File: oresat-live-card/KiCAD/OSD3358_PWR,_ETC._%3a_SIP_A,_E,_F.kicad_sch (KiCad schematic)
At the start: 53 parts, among them Q1 MMBT2907, U10 TLVH431, U18 RCLAMP0504FB, U4 SN74LVC1G07DCK, U7 OSD3358-512M-BSM

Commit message: Schematic update for V1.2, still a few outstanding TODOs
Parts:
- TP102, TP109, TP110, TP112, TP121, TP129, TP130, TP132, TP136, TP14, TP140, TP145, TP150, TP151, TP154, TP155, TP156, TP157, TP160, TP161, TP164, TP165, TP166, TP167, TP172, TP173, TP2, TP25, TP3, TP4, TP9: footprint oresat-live-card:PAD.03X.04 -> oresat-live-card:2MM-TEST-POINT; symbol oresat-live-card-eagle-import:TEST-POINT3X4 -> oresat-live-card-eagle-import:TEST-POINT
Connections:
- net GND: now also U7.D8 (DGND@1), U7.D9 (DGND@2), U7.E10 (DGND@8), U7.E11 (DGND@9), U7.E12 (DGND@10), U7.E5 (DGND@3), U7.E6 (DGND@4), U7.E7 (DGND@5), U7.E8 (DGND@6), U7.E9 (DGND@7), U7.F12 (DGND@12), U7.F5 (DGND@11), U7.G12 (DGND@14), U7.G5 (DGND@13), U7.H12 (DGND@17), U7.H13 (DGND@18), U7.H4 (DGND@15), U7.H5 (DGND@16), U7.J12 (DGND@21), U7.J13 (DGND@22), U7.J4 (DGND@19), U7.J5 (DGND@20), U7.K12 (DGND@24), U7.K5 (DGND@23), U7.L12 (DGND@26), U7.L5 (DGND@25), U7.M10 (DGND@32), U7.M11 (DGND@33), U7.M12 (DGND@34), U7.M5 (DGND@27), U7.M6 (DGND@28), U7.M7 (DGND@29), U7.M8 (DGND@30), U7.M9 (DGND@31), U7.N8 (DGND@35), U7.N9 (DGND@36); no longer U7.F8 (SYS_VDD3_3P3V@1), U7.G8 (SYS_VDD3_3P3V@2), U7.G9 (VDDSHV5), U7.H8 (SYS_VDD3_3P3V@4), U7.H9 (VDDSHV6), U7.J7 (SYS_VDD3_3P3V@5), U7.J9 (VDDSHV1), U7.K8 (SYS_VDD3_3P3V@7), U7.K9 (VDDSHV2), U7.L4 (PMIC_NWAKEUP), U7.L8 (SYS_VDD3_3P3V@8), U7.L9 (VDDSHV3), U7.M13 (PMIC_NRESET), U7.N11 (PMIC_PWR_EN), U7.N4 (PMIC_LDO_PGOOD), U7.N5 (RTC_PWRONRSTN), U7.T11 (PMIC_PB_IN)
- net at TP154.1: now also U7.G4 (VDD_CORE)
- net at TP150.1: now also U7.J6 (NC@2)
- net at TP172.1: now also U7.D12 (NC@1)
- net at TP145.1: now also U7.K4 (NC@3)
- net at TP160.1: now also U7.F13 (VDD_MPU)
- net at TP157.1: now also U7.H6 (VPP)
- net at TP166.1: now also U7.G13 (VDDS_PLL)
- net at TP173.1: now also U7.D5 (CAP_VDD_RTC)
- net at TP156.1: now also U7.F4 (VDDS_DDR)

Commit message: BOM and minor cosmetic schematic updates
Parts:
- C13, C14: value 22uF -> 22u; symbol oresat-live-card-eagle-import:C-EUC1210 -> Device:C_Small; Distributor (none) -> DigiKey; MPN (none) -> CGA6P1X7R1C226M250AC
- C18, C41: value 0.1uF -> 100n; footprint oresat-live-card:.0603-A -> Resistor_SMD:R_0603_1608Metric; symbol oresat-live-card-eagle-import:C-EU0603-A -> Device:C_Small; Distributor (none) -> DigiKey; MPN (none) -> CL10B104KB8WPNC
- D1: Distributor (none) -> DigiKey; MPN (none) -> 150060GS75020
- Q1: Distributor (none) -> DigiKey; MPN (none) -> MMBT2907A-7-F
- R1: footprint oresat-live-card:.0603-A -> Resistor_SMD:R_0603_1608Metric; Distributor (none) -> DigiKey; MPN (none) -> ERJ-3EKF4701V
- R15, R28: footprint oresat-live-card:.0603-A -> Resistor_SMD:R_0603_1608Metric; Distributor (none) -> DigiKey; MPN (none) -> ERJ-3EKF1002V
- R23: footprint oresat-live-card:.0603-A -> Resistor_SMD:R_0603_1608Metric; Distributor (none) -> DigiKey; MPN (none) -> ERJ-3EKF4990V
- R31: footprint oresat-live-card:.0603-A -> Resistor_SMD:R_0603_1608Metric; Distributor (none) -> DigiKey; MPN (none) -> ERJ-3EKF4022V
- R73, R74, R75: footprint oresat-live-card:.0603-A -> Resistor_SMD:R_0603_1608Metric; Distributor (none) -> DigiKey; MPN (none) -> ERJ-3EKF1000V
- TP102, TP109, TP110, TP121, TP129, TP130, TP132, TP136, TP14, TP140, TP145, TP150, TP154, TP156, TP157, TP160, TP161, TP164, TP165, TP166, TP167, TP172, TP173, TP2, TP25, TP3, TP4, TP9: footprint oresat-live-card:2MM-TEST-POINT -> oresat-live-card:PAD.03X.04
- TP112, TP151, TP155: value TEST-POINT3X4 -> TEST-POINT
- U10: Distributor (none) -> DigiKey; MPN (none) -> TLVH431BQDBZRQ1
- U18: Distributor (none) -> DigiKey; MPN (none) -> RCLAMP0504FBTCT
- U4: Distributor (none) -> DigiKey; MPN (none) -> SN74LVC1G07DCK3
- U7: Distributor (none) -> DigiKey; MPN (none) -> OSD3358-512M-BSM
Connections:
- net 3.3VA is gone; now on net PWR: C41.1, JP101.1, TP165.1, U18.5 (VCC), U7.F8 (SYS_VDD3_3P3V@1), U7.F9 (VDDSHV4), U7.G8 (SYS_VDD3_3P3V@2), U7.G9 (VDDSHV5), U7.H7 (SYS_VDD3_3P3V@3), U7.H8 (SYS_VDD3_3P3V@4), U7.H9 (VDDSHV6), U7.J7 (SYS_VDD3_3P3V@5), U7.J8 (SYS_VDD3_3P3V@6), U7.J9 (VDDSHV1), U7.K8 (SYS_VDD3_3P3V@7), U7.K9 (VDDSHV2), U7.L8 (SYS_VDD3_3P3V@8), U7.L9 (VDDSHV3)
- net 5V is gone; now on net PWR: C14.1, U7.P10 (VIN_AC@1), U7.R10 (VIN_AC@2), U7.T10 (VIN_AC@3)
- net VDD is gone; now on net PWR: TP3.1, U7.K6 (SYS_VOUT@1), U7.K7 (SYS_VOUT@2), U7.L6 (SYS_VOUT@3), U7.L7 (SYS_VOUT@4)
- net 3.3V renamed PWR
- net N$53: no longer names the net of C18.1, JP104.1, TP14.1, TP164.1, U4.5 (VCC), U7.K11 (SYS_RTC_1P8V@1), U7.L11 (SYS_RTC_1P8V@2)
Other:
- note removed: "" ""
- moved on the sheet: TP110

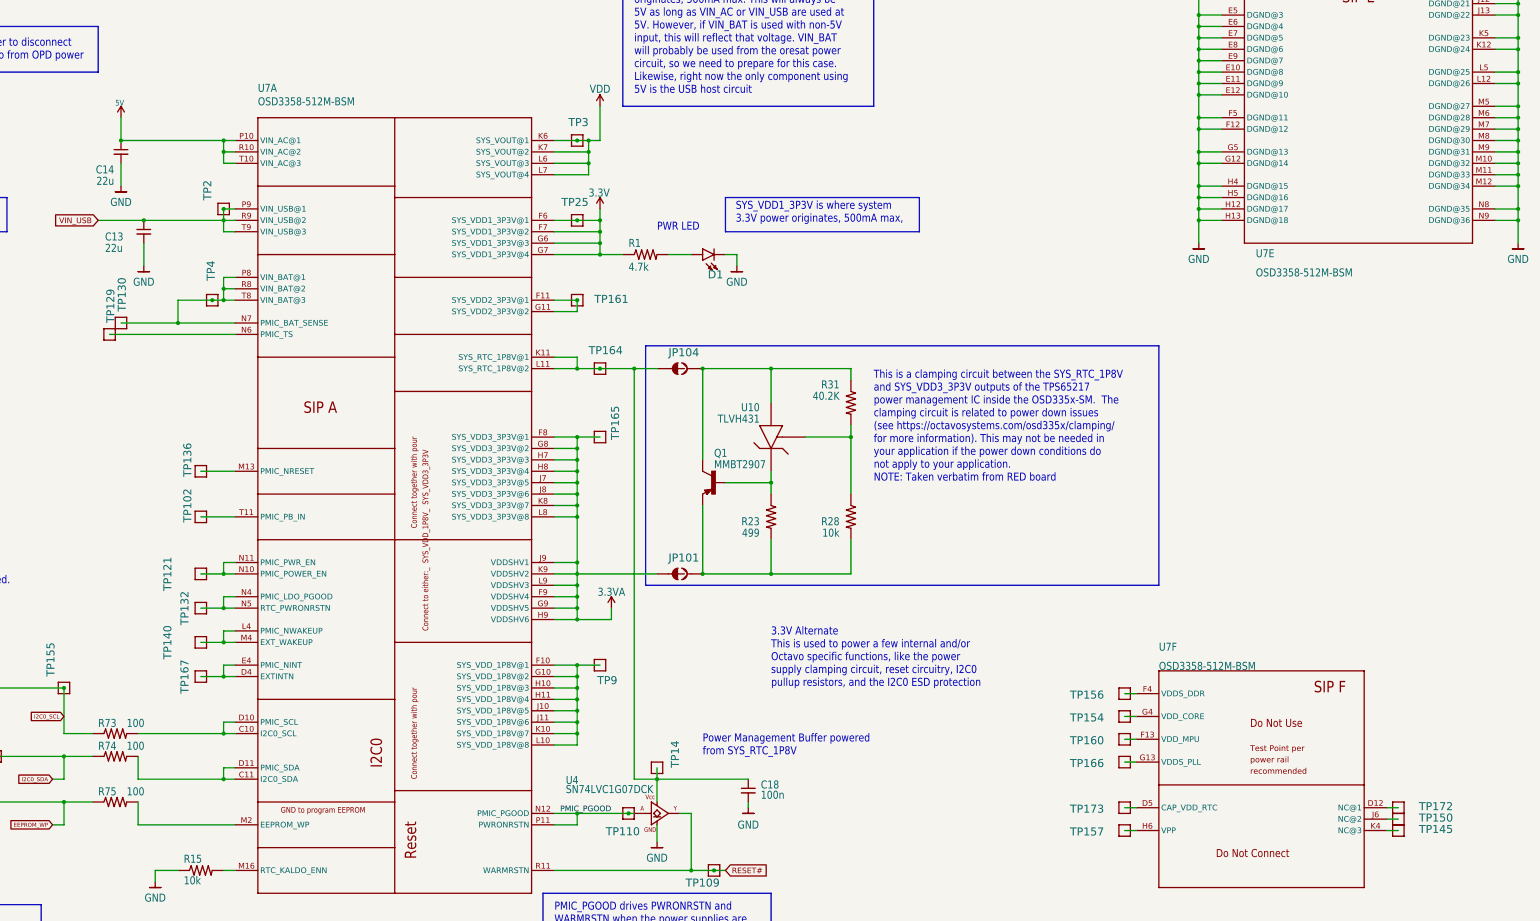
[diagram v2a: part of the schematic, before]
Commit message: updated schematic with new 5.5V reg
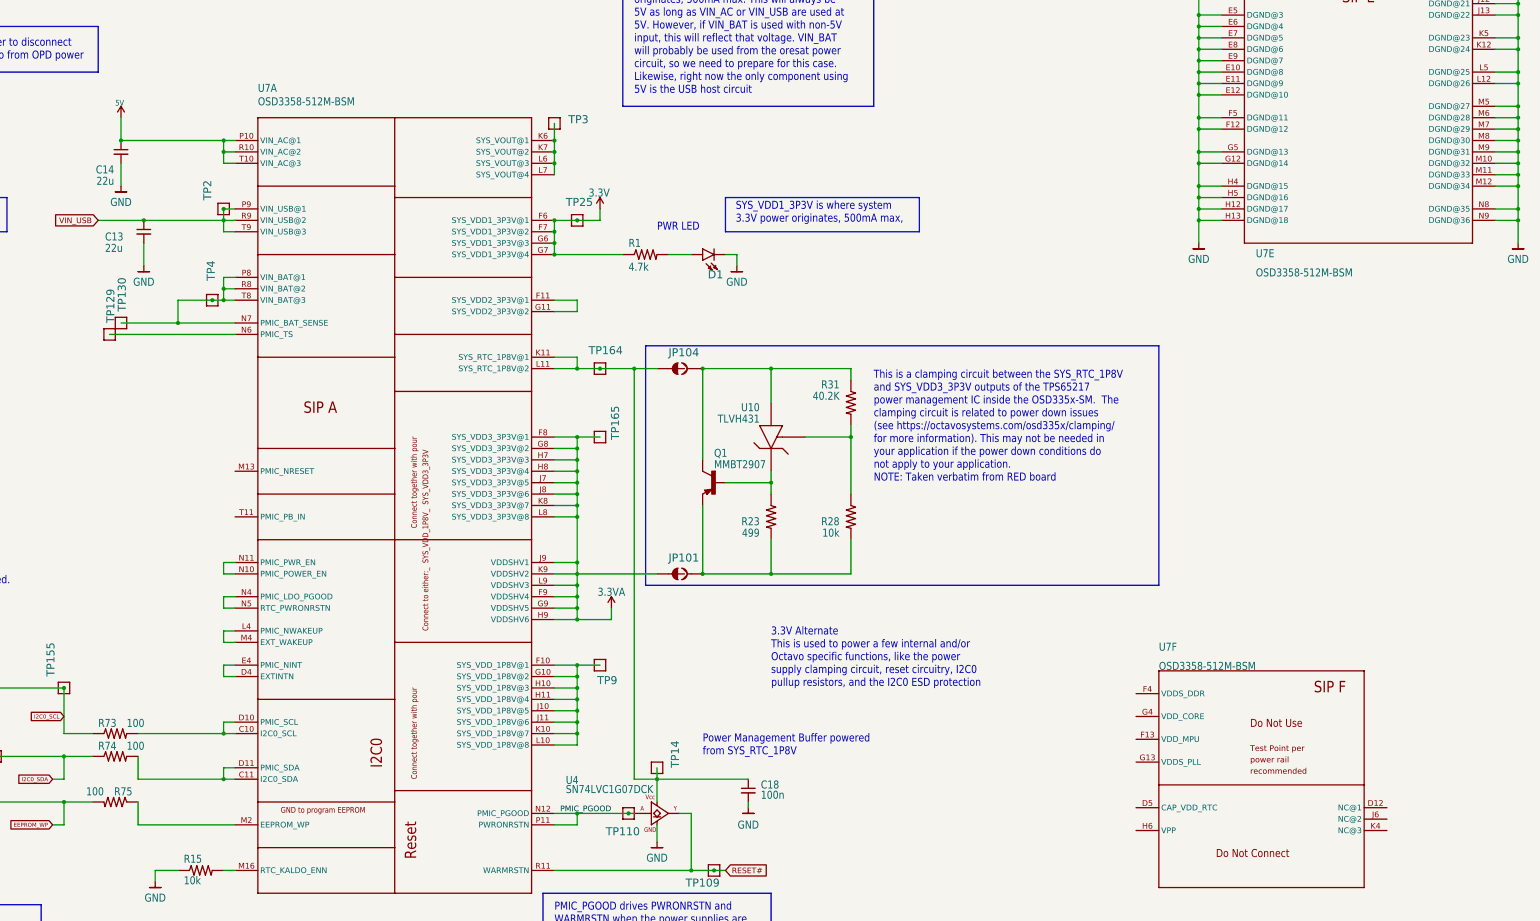
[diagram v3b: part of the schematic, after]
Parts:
- removed TP102, TP121, TP132, TP136, TP140, TP145, TP150, TP154, TP156, TP157, TP160, TP161, TP166, TP167, TP172, TP173: TEST-POINT3X4, oresat-live-card:PAD.03X.04, symbol oresat-live-card-eagle-import:TEST-POINT
- JP101, JP104: footprint oresat-live-card:SMT-JUMPER_2_NC_TRACE_SILK -> Jumper:SolderJumper-2_P1.3mm_Bridged_RoundedPad1.0x1.5mm
- TP112, TP151, TP155: footprint oresat-live-card:2MM-TEST-POINT -> oresat-live-card:PAD.03X.04
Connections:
- net EEPROM_WP: now also R75.2; no longer R75.1
- net at U7.M2 (EEPROM_WP): now also R75.1; no longer R75.2
- net PWR renamed 3.3VA
- net 3.3VA: no longer C14.1, R1.1, TP25.1, TP3.1, U7.F6 (SYS_VDD1_3P3V@1), U7.F7 (SYS_VDD1_3P3V@2), U7.G6 (SYS_VDD1_3P3V@3), U7.G7 (SYS_VDD1_3P3V@4), U7.K6 (SYS_VOUT@1), U7.K7 (SYS_VOUT@2), U7.L6 (SYS_VOUT@3), U7.L7 (SYS_VOUT@4), U7.P10 (VIN_AC@1), U7.R10 (VIN_AC@2), U7.T10 (VIN_AC@3)
- new net: TP3.1, U7.K6 (SYS_VOUT@1), U7.K7 (SYS_VOUT@2), U7.L6 (SYS_VOUT@3), U7.L7 (SYS_VOUT@4)
- new net 3.3V: R1.1, TP25.1, U7.F6 (SYS_VDD1_3P3V@1), U7.F7 (SYS_VDD1_3P3V@2), U7.G6 (SYS_VDD1_3P3V@3), U7.G7 (SYS_VDD1_3P3V@4)
- new net 5V: C14.1, U7.P10 (VIN_AC@1), U7.R10 (VIN_AC@2), U7.T10 (VIN_AC@3)
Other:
- moved on the sheet: TP25, TP3

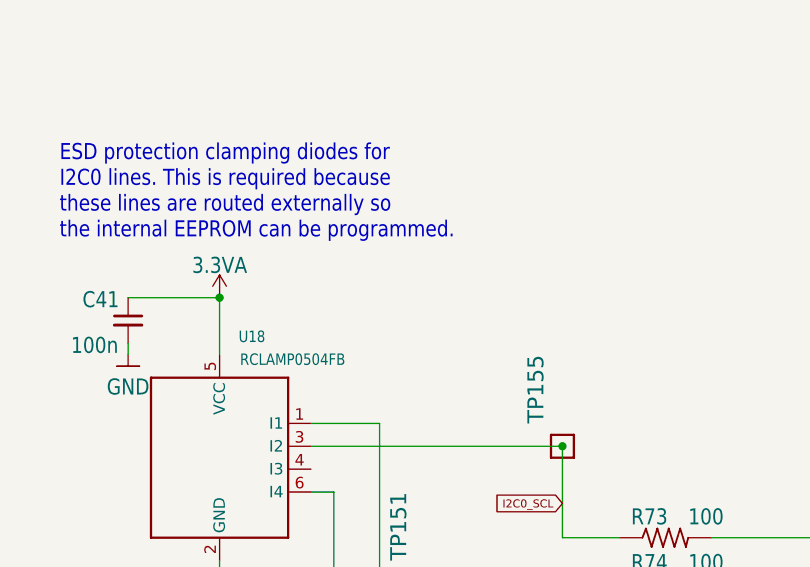
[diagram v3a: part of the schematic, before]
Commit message: Board updates for V1.2, more routing.  Design review 1
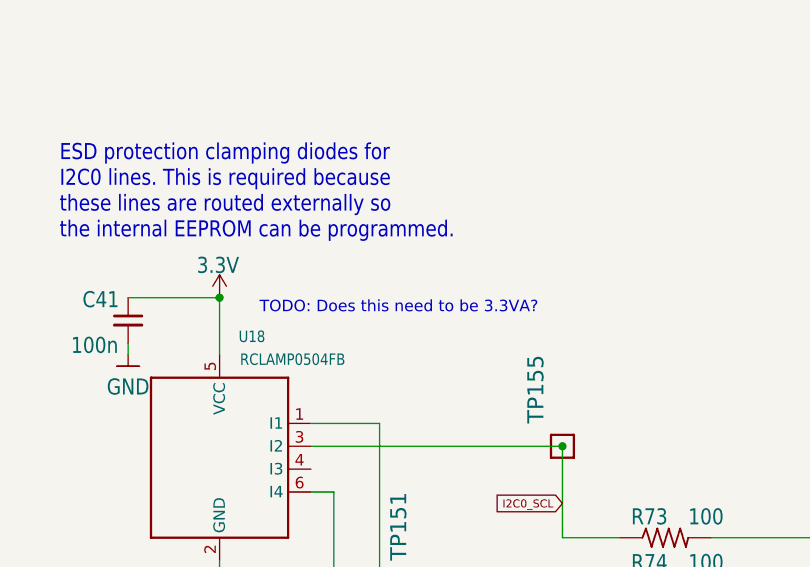
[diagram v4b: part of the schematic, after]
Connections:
- net 3.3V: now also C41.1, U18.5 (VCC)
- net 3.3VA: no longer C41.1, U18.5 (VCC)
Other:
- note added: "TODO: Does this need to be 3.3VA?"
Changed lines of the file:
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@@
   (junction (at 250.19 127) (diameter 0) (color 0 0 0 0)
   )
+  (junction (at 327.66 58.42) (diameter 0) (color 0 0 0 0)
+  )
+  (junction (at 398.78 66.04) (diameter 0) (color 0 0 0 0)
+  )
+  (junction (at 189.23 137.16) (diameter 0) (color 0 0 0 0)
+  )
+  (junction (at 189.23 185.42) (diameter 0) (color 0 0 0 0)
+  )
+  (junction (at 189.23 144.78) (diameter 0) (color 0 0 0 0)
+  )
+  (junction (at 189.23 132.08) (diameter 0) (color 0 0 0 0)
+  )
+  (junction (at 189.23 210.82) (diameter 0) (color 0 0 0 0)
+  )
+  (junction (at 398.78 40.64) (diameter 0) (color 0 0 0 0)
+  )
+  (junction (at 100.33 101.6) (diameter 0) (color 0 0 0 0)
+  )
+  (junction (at 189.23 160.02) (diameter 0) (color 0 0 0 0)
+  )
+  (junction (at 327.66 38.1) (diameter 0) (color 0 0 0 0)
+  )
+  (junction (at 398.78 60.96) (diameter 0) (color 0 0 0 0)
+  )
+  (junction (at 189.23 157.48) (diameter 0) (color 0 0 0 0)
+  )
+  (junction (at 74.93 182.88) (diameter 0) (color 0 0 0 0)
+  )
+  (junction (at 184.15 81.28) (diameter 0) (color 0 0 0 0)
+  )
+  (junction (at 110.49 193.04) (diameter 0) (color 0 0 0 0)
+  )
+  (junction (at 398.78 48.26) (diameter 0) (color 0 0 0 0)
+  )
+  (junction (at 327.66 63.5) (diameter 0) (color 0 0 0 0)
+  )
+  (junction (at 398.78 58.42) (diameter 0) (color 0 0 0 0)
+  )
+  (junction (at 398.78 45.72) (diameter 0) (color 0 0 0 0)
+  )
+  (junction (at 110.49 203.2) (diameter 0) (color 0 0 0 0)
+  )
+  (junction (at 327.66 66.04) (diameter 0) (color 0 0 0 0)
+  )
   (junction (at 36.83 166.37) (diameter 0) (color 0 0 0 0)
-  )
-  (junction (at 327.66 58.42) (diameter 0) (color 0 0 0 0)
-  )
-  (junction (at 398.78 66.04) (diameter 0) (color 0 0 0 0)
-  )
-  (junction (at 189.23 137.16) (diameter 0) (color 0 0 0 0)
-  )
-  (junction (at 189.23 185.42) (diameter 0) (color 0 0 0 0)
-  )
-  (junction (at 189.23 144.78) (diameter 0) (color 0 0 0 0)
-  )
-  (junction (at 189.23 132.08) (diameter 0) (color 0 0 0 0)
-  )
-  (junction (at 189.23 210.82) (diameter 0) (color 0 0 0 0)
-  )
-  (junction (at 398.78 40.64) (diameter 0) (color 0 0 0 0)
-  )
-  (junction (at 100.33 101.6) (diameter 0) (color 0 0 0 0)
-  )
-  (junction (at 189.23 160.02) (diameter 0) (color 0 0 0 0)
-  )
-  (junction (at 327.66 38.1) (diameter 0) (color 0 0 0 0)
-  )
-  (junction (at 398.78 60.96) (diameter 0) (color 0 0 0 0)
-  )
-  (junction (at 189.23 157.48) (diameter 0) (color 0 0 0 0)
-  )
-  (junction (at 74.93 182.88) (diameter 0) (color 0 0 0 0)
-  )
-  (junction (at 184.15 81.28) (diameter 0) (color 0 0 0 0)
-  )
-  (junction (at 110.49 193.04) (diameter 0) (color 0 0 0 0)
-  )
-  (junction (at 398.78 48.26) (diameter 0) (color 0 0 0 0)
-  )
-  (junction (at 327.66 63.5) (diameter 0) (color 0 0 0 0)
-  )
-  (junction (at 398.78 58.42) (diameter 0) (color 0 0 0 0)
-  )
-  (junction (at 398.78 45.72) (diameter 0) (color 0 0 0 0)
-  )
-  (junction (at 110.49 203.2) (diameter 0) (color 0 0 0 0)
-  )
-  (junction (at 327.66 66.04) (diameter 0) (color 0 0 0 0)
   )
   (junction (at 398.78 53.34) (diameter 0) (color 0 0 0 0)
@@
     (at 19.05 160.02 0)
     (effects (font (size 1.778 1.5113)) (justify left bottom))
+  )
+  (text "TODO: Does this need to be 3.3VA?\n" (at 41.275 168.275 0)
+    (effects (font (size 1.27 1.27)) (justify left bottom))
   )
   (text "RTC_KALDO_ENN is grounded thru a 10K ohm resistor so that\nthe internal RTC LDO is enabled and CAP_VDD_RTC does not\nneed to be connected to VDD_CORE."
@@
     (pin "6")
   )
+  (symbol (lib_id "OreSat-Power:3.3V") (at 36.83 166.37 0) (unit 1)
+    (in_bom yes) (on_board yes)
+    (property "Reference" "#3V?" (id 0) (at 36.83 166.37 0)
+      (effects (font (size 1.27 1.27)) hide)
+    )
+    (property "Value" "3.3V" (id 1) (at 34.29 163.83 0)
+      (effects (font (size 1.778 1.5113)) (justify left bottom))
+    )
+    (property "Footprint" "oresat-live-card:" (id 2) (at 36.83 166.37 0)
+      (effects (font (size 1.27 1.27)) hide)
+    )
+    (property "Datasheet" "" (id 3) (at 36.83 166.37 0)
+      (effects (font (size 1.27 1.27)) hide)
+    )
+    (pin "1")
+  )
   (symbol (lib_id "oresat-live-card-eagle-import:TEST-POINT") (at 184.15 57.15 90) (unit 1)
     (in_bom yes) (on_board yes)
@@
       (effects (font (size 1.27 1.27)) hide)
     )
-    (pin "1")
-  )
-  (symbol (lib_id "OreSat-Power:3.3VA") (at 36.83 166.37 0) (unit 1)
-    (in_bom yes) (on_board yes)
-    (property "Reference" "#3V3A01" (id 0) (at 36.83 166.37 0)
-      (effects (font (size 1.27 1.27)) hide)
-    )
-    (property "Value" "3.3VA" (id 1) (at 36.83 163.83 0)
-      (effects (font (size 1.778 1.5113)) (justify bottom))
-    )
-    (property "Footprint" "oresat-live-card:" (id 2) (at 36.83 166.37 0)
-      (effects (font (size 1.27 1.27)) hide)
-    )
-    (property "Datasheet" "" (id 3) (at 36.83 166.37 0)
-      (effects (font (size 1.27 1.27)) hide)
-    )
